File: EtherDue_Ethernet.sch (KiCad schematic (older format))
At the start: 33 parts, among them IC601 W5100, Q601 2N7002, U602 HY931147C, U603 APX811-31UG-7, X601 TXC 7A 25MHz 18pF

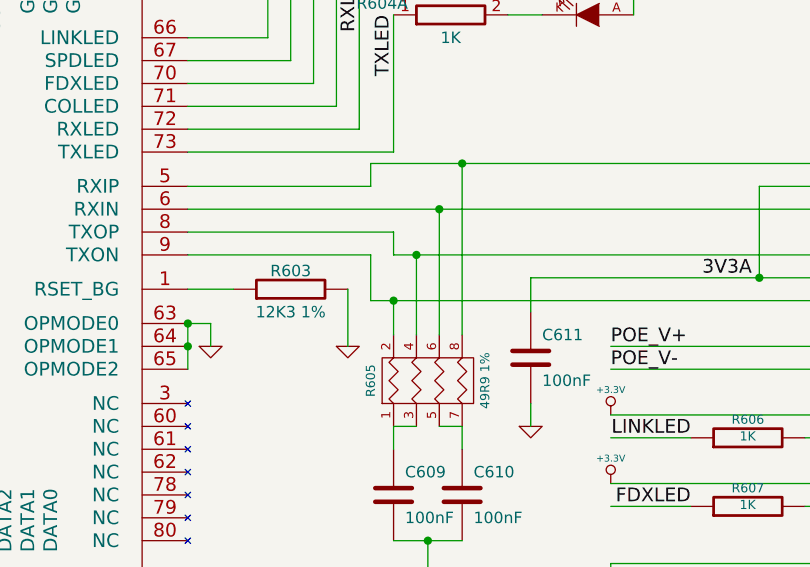
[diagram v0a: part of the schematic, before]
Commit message: Fix footprint association on resistor network for RJ45 connection
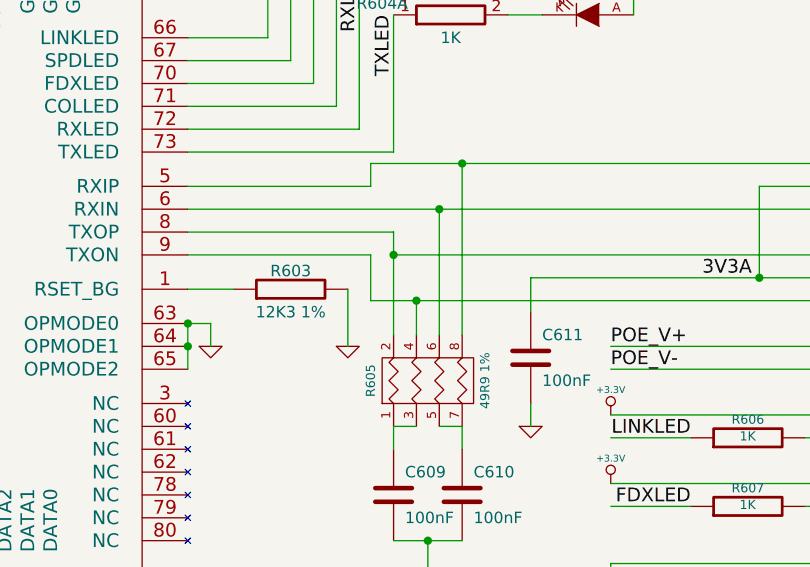
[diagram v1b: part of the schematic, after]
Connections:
- wire segments 144 -> 143
